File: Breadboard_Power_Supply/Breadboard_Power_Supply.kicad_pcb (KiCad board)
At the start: 2 copper layers, 35 x 52.2 mm, 17 parts, among them J1 Barrel_Jack_Switch, J2 Conn_01x03_Pin, J3 Conn_01x02_Pin, J4 Screw_Terminal_01x02, J5 Screw_Terminal_01x02, J6 Conn_01x03_Pin, J7 Conn_01x02_Pin, SW1 SW_SPDT, U1 LM7805_TO220, U2 LM317_TO-220

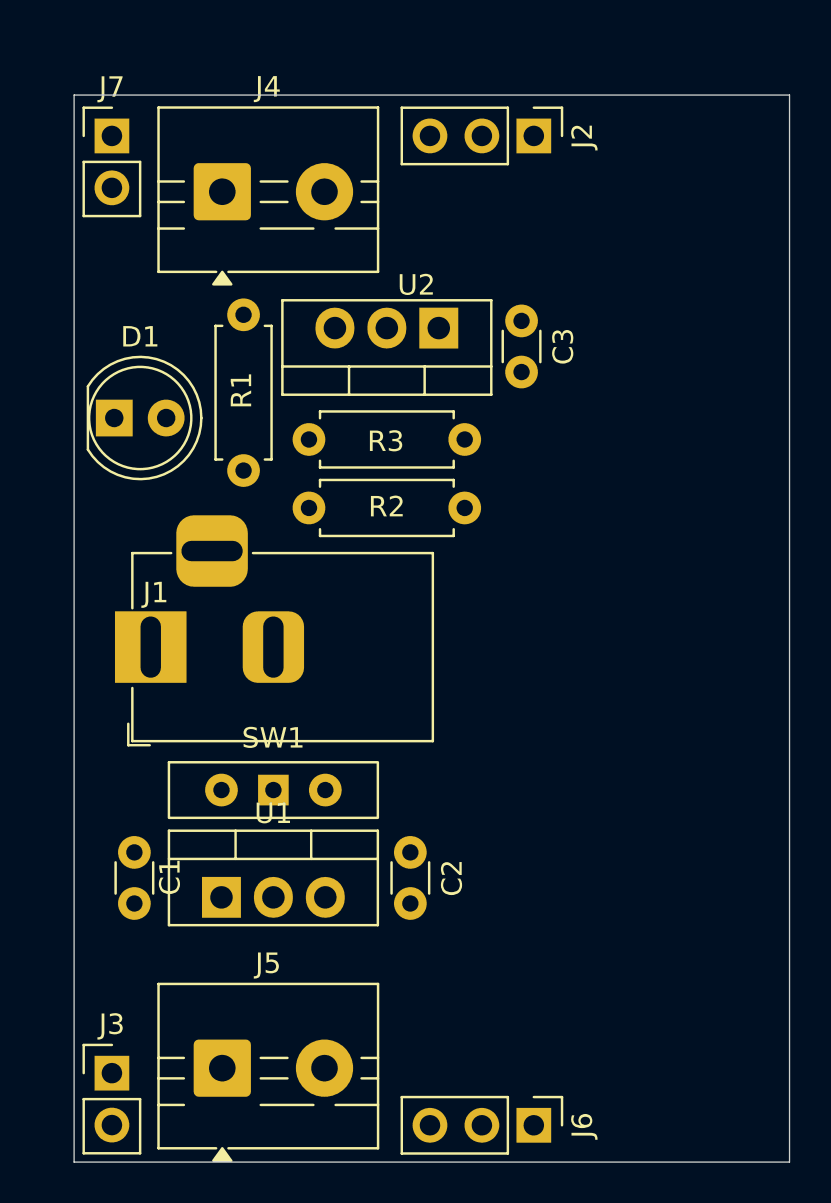
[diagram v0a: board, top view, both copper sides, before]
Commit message: Completed BreadBoard Power Supply Project
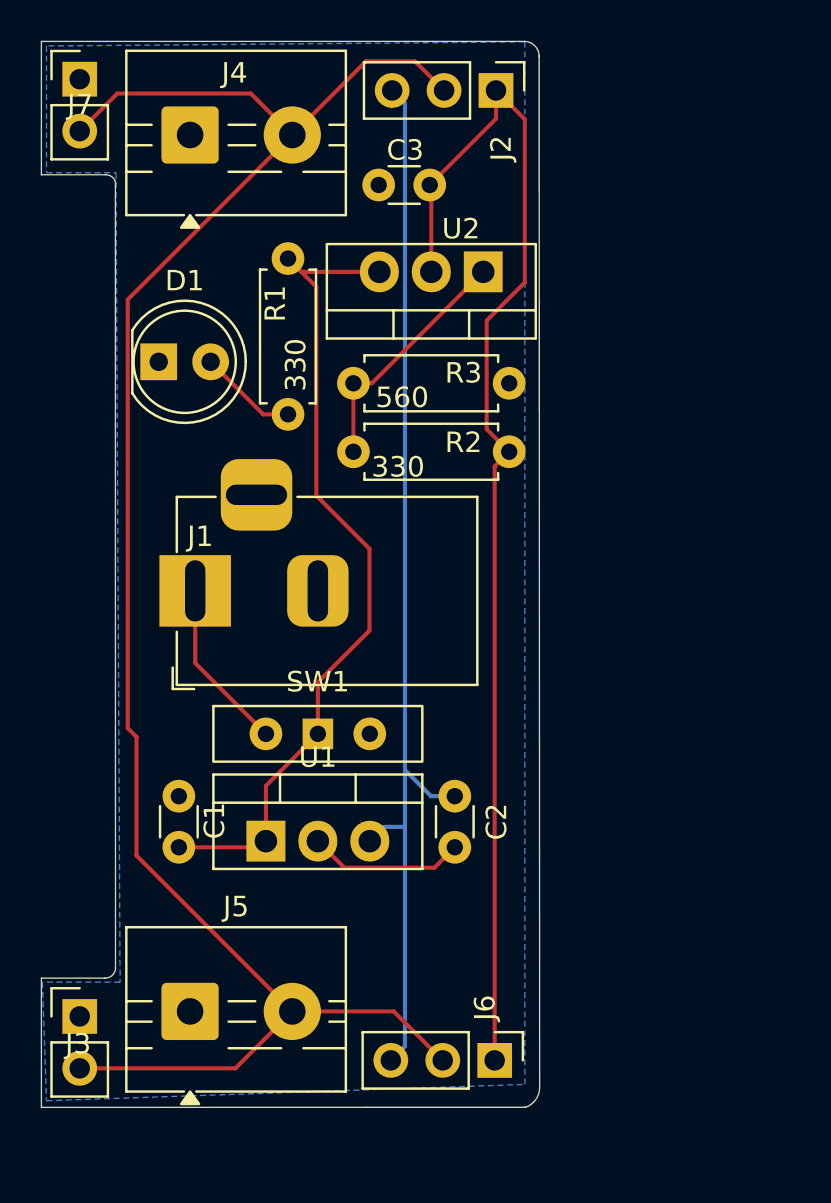
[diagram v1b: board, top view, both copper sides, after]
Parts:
- moved C3 8.02 mm to (155.3, 38.0), turned to 180 degrees
- moved J6 3.71 mm to (158.5, 80.8)
- moved D1 3.51 mm to (142.1, 46.6)
- moved J1 3.51 mm to (143.9, 57.9)
- moved R2 3.51 mm to (159.2, 51.0)
- moved R3 3.51 mm to (151.6, 47.7)
- moved SW1 3.51 mm to (149.9, 64.8)
- moved U1 3.51 mm to (147.3, 70.1)
- moved U2 3.51 mm to (158.0, 42.2)
- moved C1 3.51 mm to (143.1, 70.4)
- moved C2 3.51 mm to (156.6, 67.9)
- moved R1 3.51 mm to (148.4, 41.6)
- moved J3 3.19 mm to (138.2, 78.7)
- moved J7 3.19 mm to (138.2, 32.8)
- moved J4 3.19 mm to (143.6, 35.6)
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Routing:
- net /PWR_OUTPUT: track 0.00 -> 91.0 mm
- net /+3.3V: track 0.00 -> 59.8 mm
- net /+5V: track 0.00 -> 53.0 mm
- net /+12V: track 0.00 -> 41.4 mm
- net Net-(U2-ADJ): track 0.00 -> 12.0 mm
- net /PWR_INPUT: track 0.00 -> 8.43 mm
- net GND: track 0.00 -> 7.65 mm
- net Net-(D1-A): track 0.00 -> 4.85 mm
- added copper zone on B.Cu, net GND
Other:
- board size 35 x 52.2 mm -> 24.4 x 52.1 mm
